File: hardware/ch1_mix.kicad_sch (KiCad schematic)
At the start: 6 parts, among them U11 TC4-19G2, U12 BAT-15-099R, U23 TC4-19G2

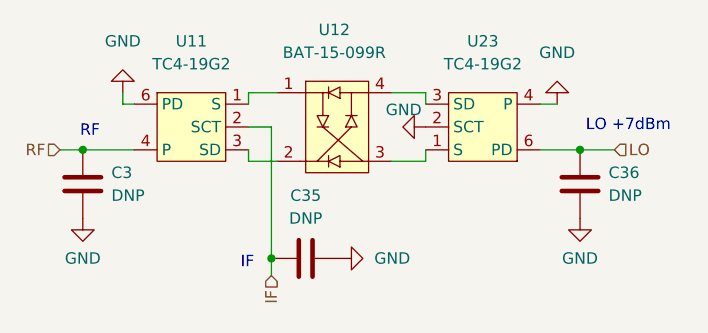
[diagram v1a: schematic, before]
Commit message: Update FEM hardware design for production version
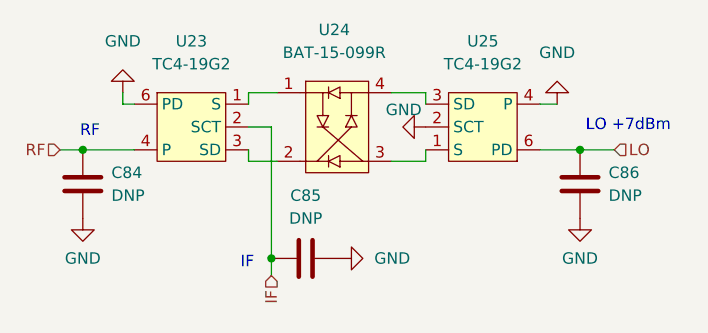
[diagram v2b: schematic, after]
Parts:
- renumbered C3 to C84, C35 to C85, C36 to C86, U11 to U23, U12 to U24, U23 to U25
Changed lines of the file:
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@@
   (symbol (lib_id "power:GND") (at 175.895 109.855 0) (unit 1)
     (in_bom yes) (on_board yes) (dnp no) (fields_autoplaced)
-    (property "Reference" "#PWR0140" (at 175.895 116.205 0)
+    (property "Reference" "#PWR0133" (at 175.895 116.205 0)
       (effects (font (size 1.27 1.27)) hide)
     )
@@
       (project "GreX Frontend"
         (path "/e63e39d7-6ac0-4ffd-8aa3-1841a4541b55/546148dc-8a5c-4178-ace4-1d6889891417/65016f85-1527-49fd-be8d-6b8d41ab58e6"
-          (reference "#PWR0140") (unit 1)
+          (reference "#PWR0133") (unit 1)
         )
       )
@@
   (symbol (lib_id "power:GND") (at 158.75 99.695 270) (unit 1)
     (in_bom yes) (on_board yes) (dnp no)
-    (property "Reference" "#PWR0135" (at 152.4 99.695 0)
+    (property "Reference" "#PWR0131" (at 152.4 99.695 0)
       (effects (font (size 1.27 1.27)) hide)
     )
@@
       (project "GreX Frontend"
         (path "/e63e39d7-6ac0-4ffd-8aa3-1841a4541b55/546148dc-8a5c-4178-ace4-1d6889891417/65016f85-1527-49fd-be8d-6b8d41ab58e6"
-          (reference "#PWR0135") (unit 1)
+          (reference "#PWR0131") (unit 1)
         )
       )
@@
   (symbol (lib_id "power:GND") (at 120.65 109.855 0) (unit 1)
     (in_bom yes) (on_board yes) (dnp no) (fields_autoplaced)
-    (property "Reference" "#PWR0141" (at 120.65 116.205 0)
+    (property "Reference" "#PWR0128" (at 120.65 116.205 0)
       (effects (font (size 1.27 1.27)) hide)
     )
@@
       (project "GreX Frontend"
         (path "/e63e39d7-6ac0-4ffd-8aa3-1841a4541b55/546148dc-8a5c-4178-ace4-1d6889891417/65016f85-1527-49fd-be8d-6b8d41ab58e6"
-          (reference "#PWR0141") (unit 1)
+          (reference "#PWR0128") (unit 1)
         )
       )
@@
   (symbol (lib_id "RF Parts:TC4-19G2") (at 165.1 100.33 180) (unit 1)
     (in_bom yes) (on_board yes) (dnp no) (fields_autoplaced)
-    (property "Reference" "U23" (at 165.1 90.17 0)
+    (property "Reference" "U25" (at 165.1 90.17 0)
       (effects (font (size 1.27 1.27)))
     )
@@
       (project "GreX Frontend"
         (path "/e63e39d7-6ac0-4ffd-8aa3-1841a4541b55/546148dc-8a5c-4178-ace4-1d6889891417/65016f85-1527-49fd-be8d-6b8d41ab58e6"
-          (reference "U23") (unit 1)
+          (reference "U25") (unit 1)
         )
       )
@@
   (symbol (lib_id "RF Parts:TC4-19G2") (at 132.715 99.06 0) (unit 1)
     (in_bom yes) (on_board yes) (dnp no) (fields_autoplaced)
-    (property "Reference" "U11" (at 132.715 90.17 0)
+    (property "Reference" "U23" (at 132.715 90.17 0)
       (effects (font (size 1.27 1.27)))
     )
@@
       (project "GreX Frontend"
         (path "/e63e39d7-6ac0-4ffd-8aa3-1841a4541b55/546148dc-8a5c-4178-ace4-1d6889891417/65016f85-1527-49fd-be8d-6b8d41ab58e6"
-          (reference "U11") (unit 1)
+          (reference "U23") (unit 1)
         )
       )
@@
   (symbol (lib_id "power:GND") (at 173.355 97.155 180) (unit 1)
     (in_bom yes) (on_board yes) (dnp no) (fields_autoplaced)
-    (property "Reference" "#PWR0136" (at 173.355 90.805 0)
+    (property "Reference" "#PWR0132" (at 173.355 90.805 0)
       (effects (font (size 1.27 1.27)) hide)
     )
@@
       (project "GreX Frontend"
         (path "/e63e39d7-6ac0-4ffd-8aa3-1841a4541b55/546148dc-8a5c-4178-ace4-1d6889891417/65016f85-1527-49fd-be8d-6b8d41ab58e6"
-          (reference "#PWR0136") (unit 1)
+          (reference "#PWR0132") (unit 1)
         )
       )
@@
   (symbol (lib_id "Device:C") (at 120.65 106.045 0) (unit 1)
     (in_bom yes) (on_board yes) (dnp no) (fields_autoplaced)
-    (property "Reference" "C3" (at 123.825 104.7749 0)
+    (property "Reference" "C84" (at 123.825 104.7749 0)
       (effects (font (size 1.27 1.27)) (justify left))
     )
@@
       (project "GreX Frontend"
         (path "/e63e39d7-6ac0-4ffd-8aa3-1841a4541b55/546148dc-8a5c-4178-ace4-1d6889891417/65016f85-1527-49fd-be8d-6b8d41ab58e6"
-          (reference "C3") (unit 1)
+          (reference "C84") (unit 1)
         )
       )
@@
   (symbol (lib_id "power:GND") (at 125.095 95.885 180) (unit 1)
     (in_bom yes) (on_board yes) (dnp no) (fields_autoplaced)
-    (property "Reference" "#PWR0137" (at 125.095 89.535 0)
+    (property "Reference" "#PWR0129" (at 125.095 89.535 0)
       (effects (font (size 1.27 1.27)) hide)
     )
@@
       (project "GreX Frontend"
         (path "/e63e39d7-6ac0-4ffd-8aa3-1841a4541b55/546148dc-8a5c-4178-ace4-1d6889891417/65016f85-1527-49fd-be8d-6b8d41ab58e6"
-          (reference "#PWR0137") (unit 1)
+          (reference "#PWR0129") (unit 1)
         )
       )
@@
   (symbol (lib_id "RF Parts:BAT-15-099R") (at 148.59 99.06 0) (unit 1)
     (in_bom yes) (on_board yes) (dnp no) (fields_autoplaced)
-    (property "Reference" "U12" (at 148.59 88.9 0)
+    (property "Reference" "U24" (at 148.59 88.9 0)
       (effects (font (size 1.27 1.27)))
     )
@@
       (project "GreX Frontend"
         (path "/e63e39d7-6ac0-4ffd-8aa3-1841a4541b55/546148dc-8a5c-4178-ace4-1d6889891417/65016f85-1527-49fd-be8d-6b8d41ab58e6"
-          (reference "U12") (unit 1)
+          (reference "U24") (unit 1)
         )
       )
@@
   (symbol (lib_id "Device:C") (at 175.895 106.045 0) (unit 1)
     (in_bom yes) (on_board yes) (dnp no) (fields_autoplaced)
-    (property "Reference" "C36" (at 179.07 104.7749 0)
+    (property "Reference" "C86" (at 179.07 104.7749 0)
       (effects (font (size 1.27 1.27)) (justify left))
     )
@@
       (project "GreX Frontend"
         (path "/e63e39d7-6ac0-4ffd-8aa3-1841a4541b55/546148dc-8a5c-4178-ace4-1d6889891417/65016f85-1527-49fd-be8d-6b8d41ab58e6"
-          (reference "C36") (unit 1)
+          (reference "C86") (unit 1)
         )
       )
@@
   (symbol (lib_id "power:GND") (at 149.225 114.3 90) (unit 1)
     (in_bom yes) (on_board yes) (dnp no) (fields_autoplaced)
-    (property "Reference" "#PWR0139" (at 155.575 114.3 0)
+    (property "Reference" "#PWR0130" (at 155.575 114.3 0)
       (effects (font (size 1.27 1.27)) hide)
     )
@@
       (project "GreX Frontend"
         (path "/e63e39d7-6ac0-4ffd-8aa3-1841a4541b55/546148dc-8a5c-4178-ace4-1d6889891417/65016f85-1527-49fd-be8d-6b8d41ab58e6"
-          (reference "#PWR0139") (unit 1)
+          (reference "#PWR0130") (unit 1)
         )
       )
@@
   (symbol (lib_id "Device:C") (at 145.415 114.3 90) (unit 1)
     (in_bom yes) (on_board yes) (dnp no) (fields_autoplaced)
-    (property "Reference" "C35" (at 145.415 107.315 90)
+    (property "Reference" "C85" (at 145.415 107.315 90)
       (effects (font (size 1.27 1.27)))
     )
@@
       (project "GreX Frontend"
         (path "/e63e39d7-6ac0-4ffd-8aa3-1841a4541b55/546148dc-8a5c-4178-ace4-1d6889891417/65016f85-1527-49fd-be8d-6b8d41ab58e6"
-          (reference "C35") (unit 1)
-        )
-      )
+          (reference "C85") (unit 1)
+        )
+      )
